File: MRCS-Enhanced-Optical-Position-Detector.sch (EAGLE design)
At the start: 15 parts, among them IC1 LM2903N, T1 PT19, T2 2N4401

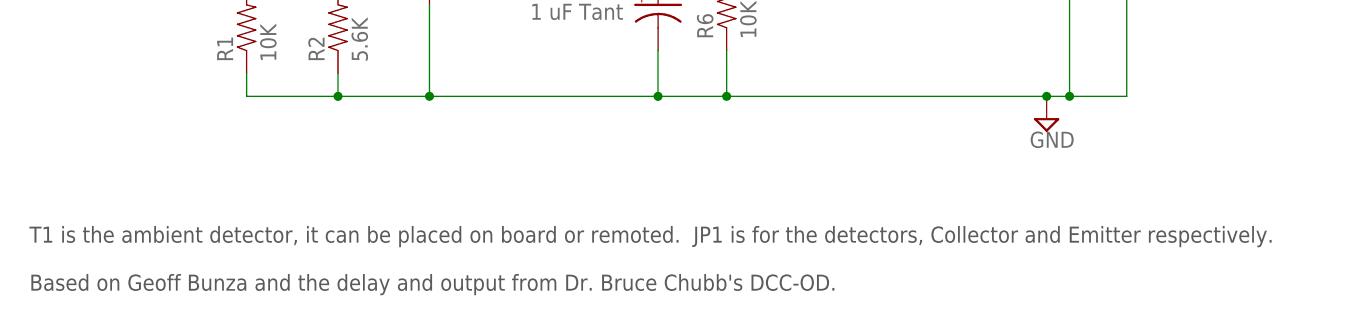
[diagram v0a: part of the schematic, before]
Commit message: clean up before panelizing
miscellaneous clean up of the file preperatory to panelizing
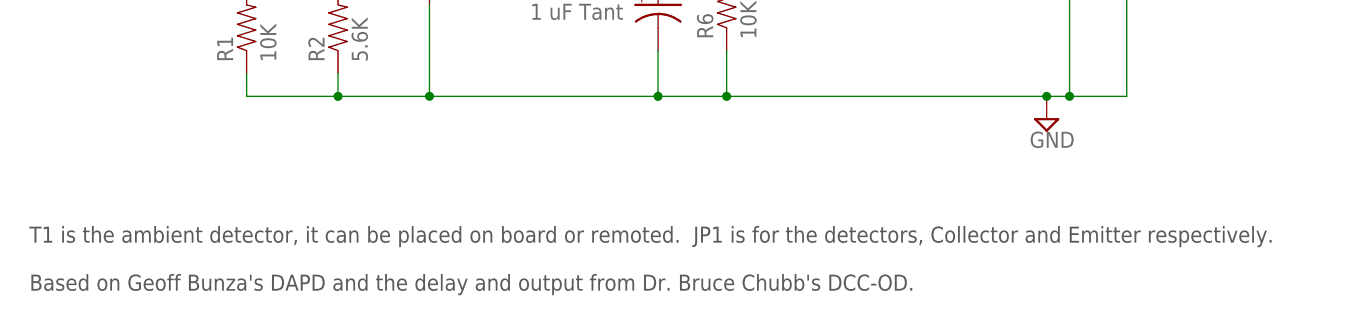
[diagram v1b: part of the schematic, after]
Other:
- note added: "T1 is the ambient detector, it can be placed on board or remoted. JP1 is for the detectors, Collector and Emitter respectively. Based on Geoff Bunza's DAPD and the delay and output from Dr. Bruce Chubb's DCC-OD."
- note removed: "T1 is the ambient detector, it can be placed on board or remoted. JP1 is for the detectors, Collector and Emitter respectively. Based on Geoff Bunza and the delay and output from Dr. Bruce Chubb's DCC-OD."
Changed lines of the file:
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@@
 <?xml version="1.0" encoding="utf-8"?>
 <!DOCTYPE eagle SYSTEM "eagle.dtd">
-<eagle version="7.3.0">
+<eagle version="7.7.0">
 <drawing>
 <settings>
@@
 <setting verticaltext="up"/>
 </settings>
-<grid distance="0.1" unitdist="inch" unit="inch" style="lines" multiple="1" display="no" altdistance="0.01" altunitdist="inch" altunit="inch"/>
+<grid distance="100" unitdist="mil" unit="mil" style="dots" multiple="1" display="yes" altdistance="50" altunitdist="mil" altunit="mil"/>
 <layers>
 <layer number="1" name="Top" color="4" fill="1" visible="no" active="no"/>
@@
 Emt 2</text>
 <text x="113.03" y="74.93" size="1.778" layer="97">T1 is the ambient detector, it can be placed on board or remoted.  JP1 is for the detectors, Collector and Emitter respectively.
-Based on Geoff Bunza and the delay and output from Dr. Bruce Chubb's DCC-OD.</text>
+Based on Geoff Bunza's DAPD and the delay and output from Dr. Bruce Chubb's DCC-OD.</text>
 </plain>
 <instances>
@@
 <segment>
 <pinref part="SUPPLY2" gate="GND" pin="GND"/>
-<pinref part="SUPPLY2" gate="GND" pin="GND"/>
 <wire x1="226.06" y1="96.52" x2="228.6" y2="96.52" width="0.1524" layer="91"/>

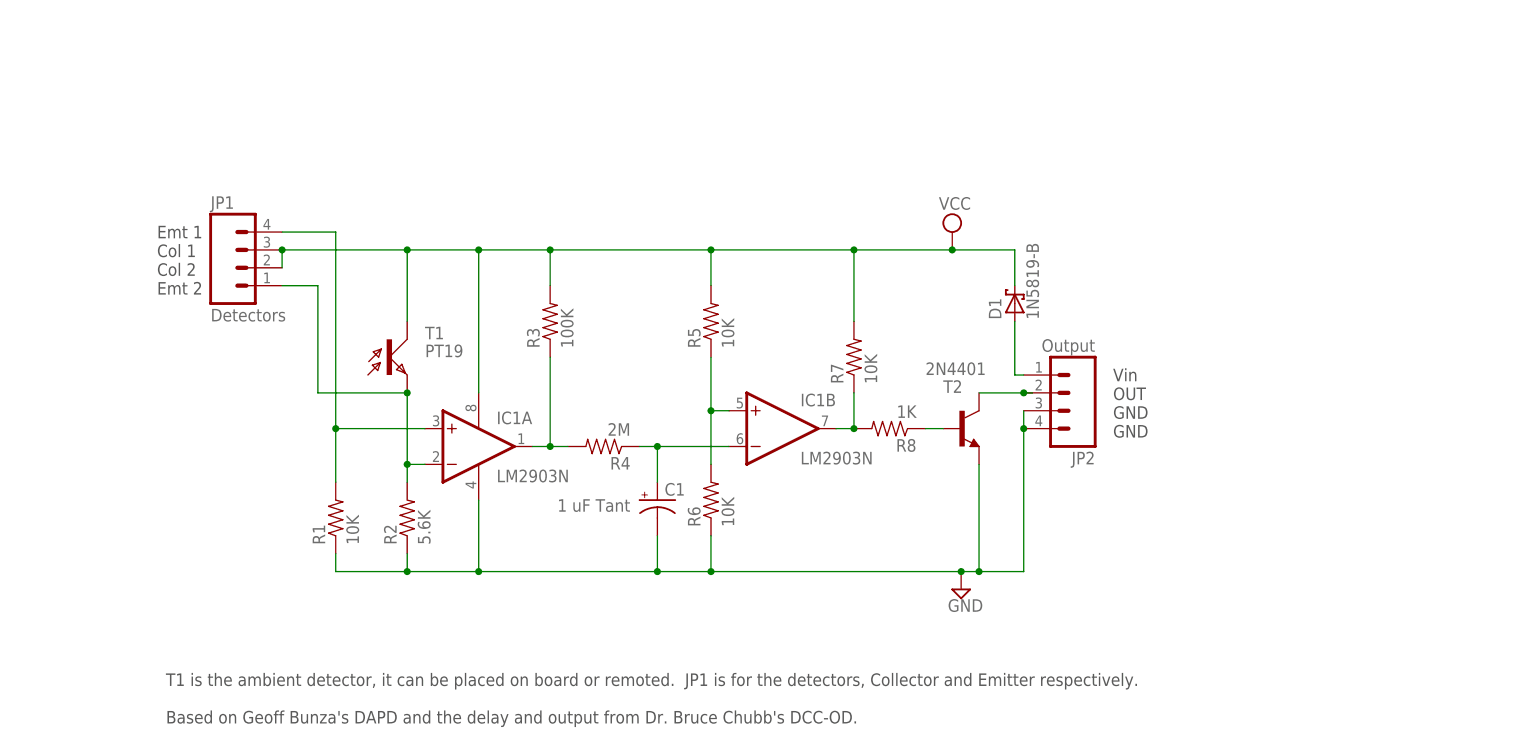
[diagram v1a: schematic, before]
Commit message: Added values for no-delay
Values for no-delay version
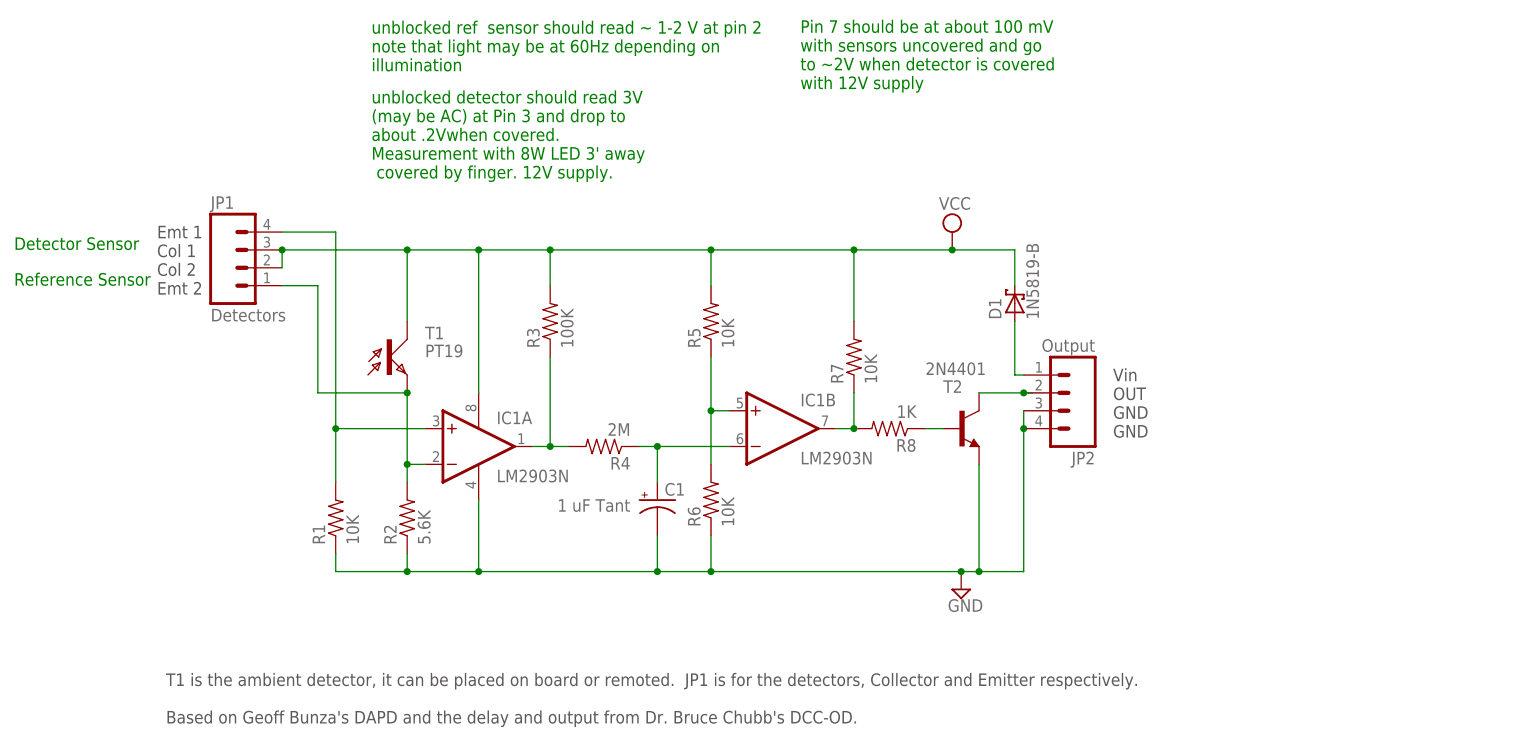
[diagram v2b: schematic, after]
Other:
- note added: "Detector Sensor"
- note added: "Pin 7 should be at about 100 mV with sensors uncovered and go to ~2V when detector is covered with 12V supply"
- note added: "Reference Sensor"
- note added: "unblocked detector should read 3V (may be AC) at Pin 3 and drop to about .2Vwhen covered. Measurement with 8W LED 3' away covered by finger. 12V supply."
- note added: "unblocked ref sensor should read ~ 1-2 V at pin 2 note that light may be at 60Hz depending on illumination"
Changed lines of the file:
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@@
 <text x="113.03" y="74.93" size="1.778" layer="97">T1 is the ambient detector, it can be placed on board or remoted.  JP1 is for the detectors, Collector and Emitter respectively.
 Based on Geoff Bunza's DAPD and the delay and output from Dr. Bruce Chubb's DCC-OD.</text>
+<text x="91.44" y="137.16" size="1.778" layer="91">Reference Sensor</text>
+<text x="91.44" y="142.24" size="1.778" layer="91">Detector Sensor</text>
+<text x="142.24" y="167.64" size="1.778" layer="91">unblocked ref  sensor should read ~ 1-2 V at pin 2
+note that light may be at 60Hz depending on
+illumination</text>
+<text x="142.24" y="152.4" size="1.778" layer="91">unblocked detector should read 3V
+(may be AC) at Pin 3 and drop to
+about .2Vwhen covered.
+Measurement with 8W LED 3' away
+ covered by finger. 12V supply.</text>
+<text x="203.2" y="165.1" size="1.778" layer="91">Pin 7 should be at about 100 mV
+with sensors uncovered and go
+to ~2V when detector is covered
+with 12V supply</text>
 </plain>
 <instances>
